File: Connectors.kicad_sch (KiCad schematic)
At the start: 23 parts, among them J1 Precidip 853-87-004-20-001101, J10 Precidip 853-87-004-20-001101, J11 FPC 0.3mm Aces 51688-0070M, J12 Precidip 853-87-004-20-001101, J13 TE 3-2363961-0 receptacle, J15 Precidip 853-87-004-20-001101, J16 TE 3-2363961-0 receptacle, J18 Precidip 852-10-004-20-001101, J2 Precidip 853-87-004-20-001101, J3 FPC 0.3mm Aces 51688-0070M, J4 Precidip 853-87-004-20-001101, J5 FPC 0.3mm Aces 51688-0070M, J6 Precidip 853-87-004-20-001101, J7 Precidip 853-87-004-20-001101, J8 FPC 0.3mm Aces 51688-0070M, J9 Precidip 853-87-004-20-001101

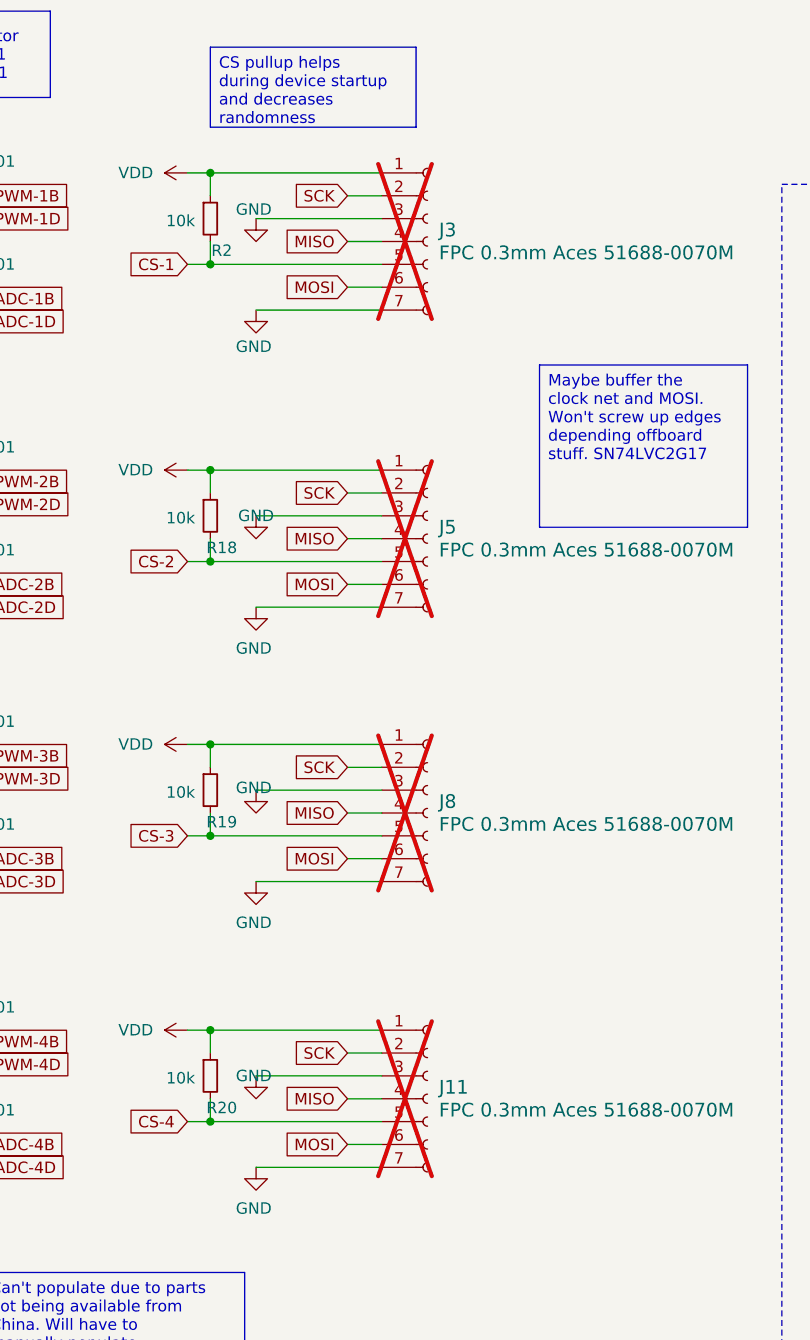
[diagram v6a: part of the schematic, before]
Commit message: Fixed BOM LCSC part numbers mostly
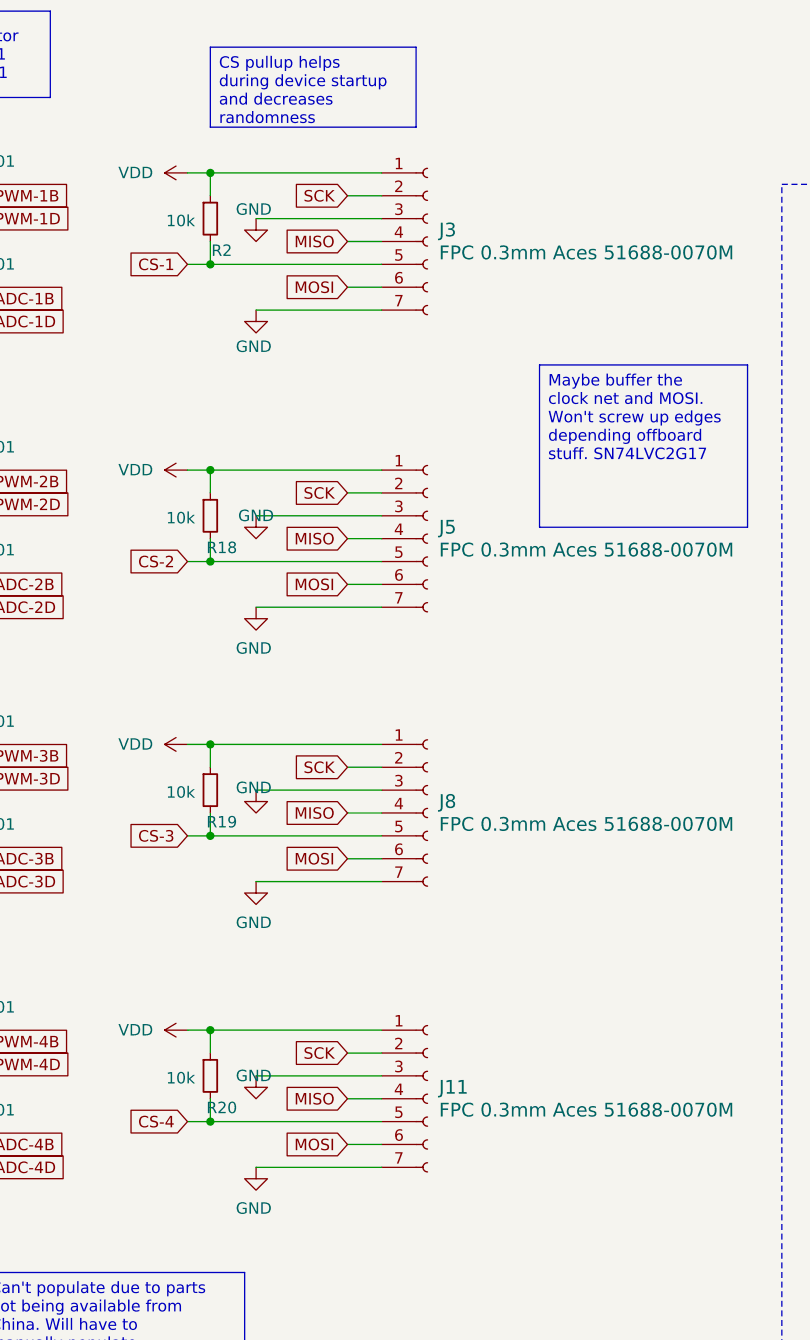
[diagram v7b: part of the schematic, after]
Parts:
- J11, J3, J5, J8: now fitted
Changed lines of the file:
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@@
 		(in_bom yes)
 		(on_board yes)
-		(dnp yes)
+		(dnp no)
 		(fields_autoplaced yes)
 		(property "Reference" "J5"
@@
 		(in_bom yes)
 		(on_board yes)
-		(dnp yes)
+		(dnp no)
 		(fields_autoplaced yes)
 		(property "Reference" "J11"
@@
 		(in_bom yes)
 		(on_board yes)
-		(dnp yes)
+		(dnp no)
 		(fields_autoplaced yes)
 		(property "Reference" "J8"
@@
 		(in_bom yes)
 		(on_board yes)
-		(dnp yes)
+		(dnp no)
 		(fields_autoplaced yes)
 		(property "Reference" "J3"

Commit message: Updated 3D models
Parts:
- J1, J10, J12, J15, J2, J4, J6, J7, J9: footprint Connector_PinHeader_1.27mm:PinHeader_2x02_P1.27mm_Horizontal -> custom_Connector:Precidip 853-87-004-20-001101
- J18: footprint Connector_PinHeader_1.27mm:PinHeader_2x02_P1.27mm_Horizontal -> custom_Connector:Precidip 852-10-004-20-001101
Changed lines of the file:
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@@
 			)
 		)
-		(property "Footprint" "Connector_PinHeader_1.27mm:PinHeader_2x02_P1.27mm_Horizontal"
+		(property "Footprint" "custom_Connector:Precidip 853-87-004-20-001101"
 			(at 33.02 115.57 0)
 			(effects
@@
 			)
 		)
-		(property "Footprint" "Connector_PinHeader_1.27mm:PinHeader_2x02_P1.27mm_Horizontal"
+		(property "Footprint" "custom_Connector:Precidip 852-10-004-20-001101"
 			(at 156.21 189.23 0)
 			(effects
@@
 			)
 		)
-		(property "Footprint" "Connector_PinHeader_1.27mm:PinHeader_2x02_P1.27mm_Horizontal"
+		(property "Footprint" "custom_Connector:Precidip 853-87-004-20-001101"
 			(at 33.02 147.32 0)
 			(effects
@@
 			)
 		)
-		(property "Footprint" "Connector_PinHeader_1.27mm:PinHeader_2x02_P1.27mm_Horizontal"
+		(property "Footprint" "custom_Connector:Precidip 853-87-004-20-001101"
 			(at 33.02 96.52 0)
 			(effects
@@
 			)
 		)
-		(property "Footprint" "Connector_PinHeader_1.27mm:PinHeader_2x02_P1.27mm_Horizontal"
+		(property "Footprint" "custom_Connector:Precidip 853-87-004-20-001101"
 			(at 33.02 53.34 0)
 			(effects
@@
 			)
 		)
-		(property "Footprint" "Connector_PinHeader_1.27mm:PinHeader_2x02_P1.27mm_Horizontal"
+		(property "Footprint" "custom_Connector:Precidip 853-87-004-20-001101"
 			(at 33.02 158.75 0)
 			(effects
@@
 			)
 		)
-		(property "Footprint" "Connector_PinHeader_1.27mm:PinHeader_2x02_P1.27mm_Horizontal"
+		(property "Footprint" "custom_Connector:Precidip 853-87-004-20-001101"
 			(at 156.21 167.64 0)
 			(effects
@@
 			)
 		)
-		(property "Footprint" "Connector_PinHeader_1.27mm:PinHeader_2x02_P1.27mm_Horizontal"
+		(property "Footprint" "custom_Connector:Precidip 853-87-004-20-001101"
 			(at 33.02 64.77 0)
 			(effects
@@
 			)
 		)
-		(property "Footprint" "Connector_PinHeader_1.27mm:PinHeader_2x02_P1.27mm_Horizontal"
+		(property "Footprint" "custom_Connector:Precidip 853-87-004-20-001101"
 			(at 33.02 85.09 0)
 			(effects
@@
 			)
 		)
-		(property "Footprint" "Connector_PinHeader_1.27mm:PinHeader_2x02_P1.27mm_Horizontal"
+		(property "Footprint" "custom_Connector:Precidip 853-87-004-20-001101"
 			(at 33.02 127 0)
 			(effects
